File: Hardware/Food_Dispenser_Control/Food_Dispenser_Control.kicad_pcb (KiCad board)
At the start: 2 copper layers, 100 x 100 mm, 63 parts, among them J1 Motor Output, J10 Conn_01x03_Pin, J2 USB_C_Receptacle_USB2.0_16P, J3 Conn_01x02_Pin, J4 Conn_01x07_Pin, J5 Conn_01x01, J6 Conn_01x01, J7 Conn_01x04_Pin, J8 Motor Output, J9 Motor Output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

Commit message: Routing
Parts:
- moved SW6 26.6 mm to (128.0, 100.0)
- moved R30 26.5 mm to (123.0, 100.0), turned to 180 degrees
- moved C12 20.1 mm to (178.0, 130.5)
- moved C17 20.0 mm to (176.5, 111.0)
- moved C16 14.9 mm to (176.5, 113.2)
- moved C11 14.6 mm to (178.0, 133.0)
- moved R14 14.6 mm to (185.5, 133.0)
- moved C24 12.3 mm to (177.0, 97.0)
- moved C23 11.9 mm to (177.0, 94.5)
- moved C10 10.8 mm to (185.5, 135.5)
- moved C15 10.6 mm to (182.5, 114.0), turned to 90 degrees
- moved C3 10.3 mm to (155.0, 142.5), turned to 90 degrees
- moved C22 9.70 mm to (185.0, 93.5), turned to 90 degrees
- moved U8 9.69 mm to (179.5, 104.0)
- moved R21 9.67 mm to (185.0, 114.0), turned to 90 degrees
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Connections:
- J1 pad 1: Net-(J1-Pin_1) -> /AOUT1
- J1 pad 2: Net-(J1-Pin_2) -> /AOUT2
- J1 pad 3: Net-(J1-Pin_3) -> /BOUT2
- J1 pad 4: Net-(J1-Pin_4) -> /BOUT1
- J7 pad 2: /INA+ -> /INA-
- J7 pad 3: /INA- -> /INA+
- J8 pad 1: Net-(J8-Pin_1) -> /AOUT1_2
- J8 pad 2: Net-(J8-Pin_2) -> /AOUT2_2
- J8 pad 3: Net-(J8-Pin_3) -> /BOUT2_2
- J8 pad 4: Net-(J8-Pin_4) -> /BOUT1_2
- J9 pad 1: Net-(J9-Pin_1) -> /AOUT1_3
- J9 pad 2: Net-(J9-Pin_2) -> /AOUT2_3
- J9 pad 3: Net-(J9-Pin_3) -> /BOUT2_3
- J9 pad 4: Net-(J9-Pin_4) -> /BOUT1_3
- U5 pad 2: Net-(J1-Pin_4) -> /AOUT1
- U5 pad 4: Net-(J1-Pin_3) -> /AOUT2
- U5 pad 5: Net-(J1-Pin_1) -> /BOUT2
- U5 pad 7: Net-(J1-Pin_2) -> /BOUT1
- U6 pad 2: Net-(J8-Pin_4) -> /AOUT1_2
- U6 pad 4: Net-(J8-Pin_3) -> /AOUT2_2
- U6 pad 5: Net-(J8-Pin_1) -> /BOUT2_2
- U6 pad 7: Net-(J8-Pin_2) -> /BOUT1_2
- U8 pad 2: Net-(J9-Pin_4) -> /AOUT1_3
- U8 pad 4: Net-(J9-Pin_3) -> /AOUT2_3
- U8 pad 5: Net-(J9-Pin_1) -> /BOUT2_3
- U8 pad 7: Net-(J9-Pin_2) -> /BOUT1_3
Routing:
- net +3.3V: track 0.00 -> 218.5 mm, vias 0 -> 5
- net /VBAT_SYS: track 0.00 -> 132.0 mm, vias 0 -> 4
- net /DIRA: track 0.00 -> 58.7 mm, vias 0 -> 4
- net /PWMA: track 0.00 -> 57.6 mm, vias 0 -> 4
- net /DIRB: track 0.00 -> 56.8 mm, vias 0 -> 4
- net /PWMB: track 0.00 -> 56.6 mm, vias 0 -> 4
- net /Sleep: track 0.00 -> 56.1 mm
- net /VBAT: track 0.00 -> 52.9 mm, vias 0 -> 2
- net /GPIO1_3: track 0.00 -> 52.8 mm
- net /GPIO1_2: track 0.00 -> 51.3 mm
- net /EN1: track 0.00 -> 50.1 mm
- net /GPIO1_1: track 0.00 -> 49.7 mm
- net /XSHUT3: track 0.00 -> 44.4 mm
- net /XSHUT2: track 0.00 -> 42.8 mm
- net /SDA: track 0.00 -> 41.5 mm
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
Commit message: Ground Plane
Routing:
- added copper zone on B.Cu, net GND
- added copper zone on F.Cu, net GND
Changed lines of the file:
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@@
 			(at -2.4 23.090001 0)
 			(layer "F.SilkS")
+			(hide yes)
 			(effects
 				(font
@@
 			(at 4.5 -8.439999 0)
 			(layer "F.SilkS")
+			(hide yes)
 			(effects
 				(font
@@
 			(at 0 -3.449999 0)
 			(layer "F.SilkS")
+			(hide yes)
 			(effects
 				(font
@@
 			(at 0 3.449999 0)
 			(layer "F.Fab")
+			(hide yes)
 			(effects
 				(font
@@
 		(net 86)
 	)
+	(zone
+		(net 1)
+		(net_name "GND")
+		(layer "F.Cu")
+		(hatch edge 0.5)
+		(connect_pads
+			(clearance 0.5)
+		)
+		(min_thickness 0.25)
+		(filled_areas_thickness no)
+		(fill yes
+			(thermal_gap 0.5)
+			(thermal_bridge_width 0.5)
+		)
+		(polygon
+			(pts
+				(xy 101 158) (xy 101 58) (xy 201 58) (xy 201 158)
+			)
+		)
+	)
+	(zone
+		(net 1)
+		(net_name "GND")
+		(layer "B.Cu")
+		(hatch edge 0.5)
+		(priority 1)
+		(connect_pads
+			(clearance 0.5)
+		)
+		(min_thickness 0.25)
+		(filled_areas_thickness no)
+		(fill yes
+			(thermal_gap 0.5)
+			(thermal_bridge_width 0.5)
+		)
+		(polygon
+			(pts
+				(xy 101 158) (xy 101 58) (xy 201 58) (xy 201 158)
+			)
+		)
+	)
 	(embedded_fonts no)

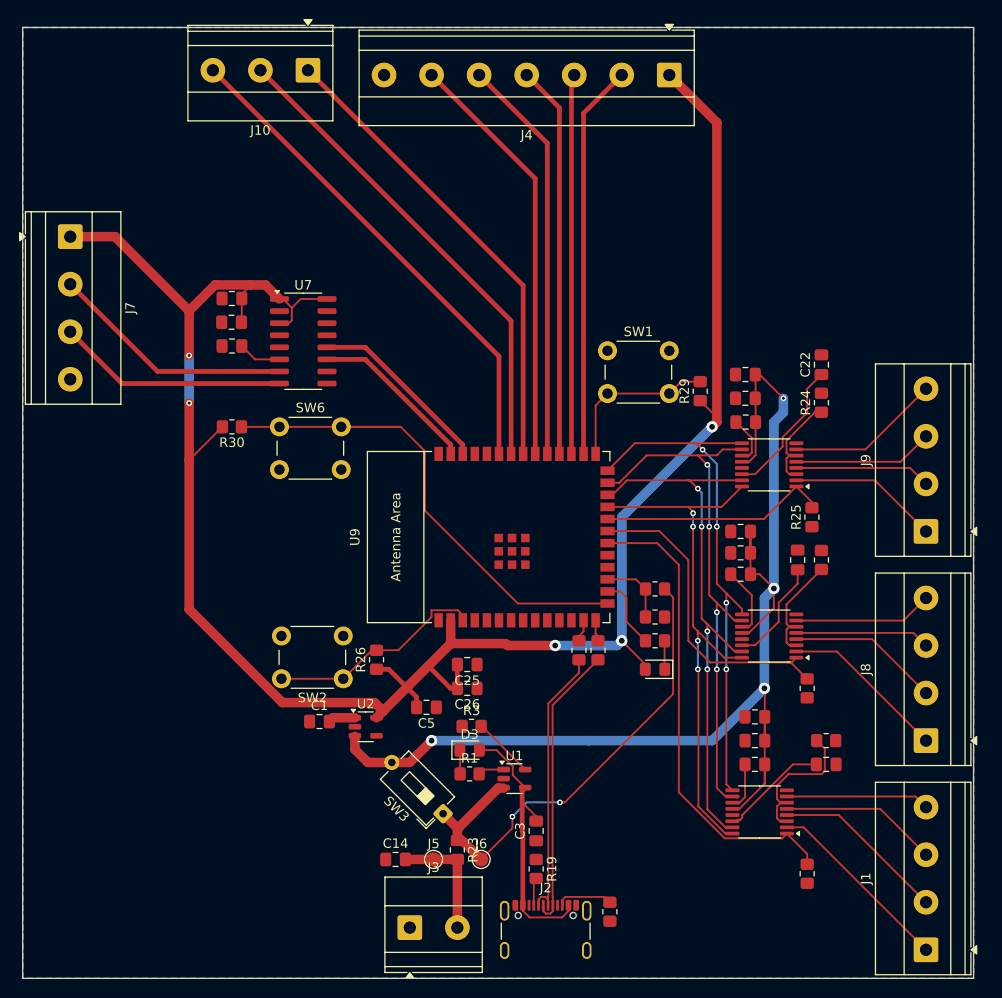
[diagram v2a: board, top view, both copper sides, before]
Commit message: Ground routing
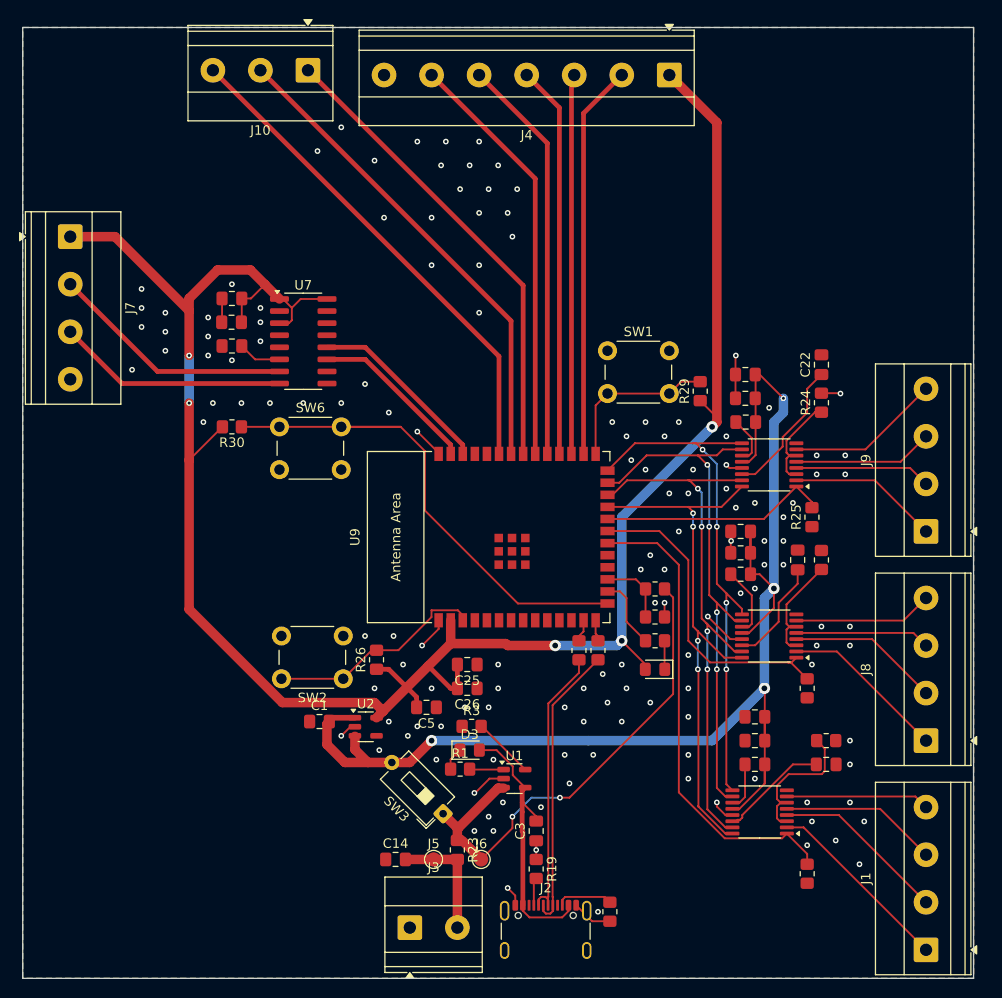
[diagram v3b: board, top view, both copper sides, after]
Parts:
- moved R1 1.12 mm to (147.0, 136.0)
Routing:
- net GND: track 0.00 -> 42.1 mm, vias 0 -> 142
- net /VBAT_SYS: track 132.0 -> 139.6 mm
- net +3.3V: track 218.5 -> 222.3 mm
- net Net-(U1-STAT): track 2.76 -> 3.59 mm

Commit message: updated hardware
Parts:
- added H1: MountingHole, MountingHole:MountingHole_3.2mm_M3, F.Cu at (196.0, 63.0)
- added H2: MountingHole, MountingHole:MountingHole_3.2mm_M3, F.Cu at (106.0, 63.0)
- added H3: MountingHole, MountingHole:MountingHole_3.2mm_M3, F.Cu at (106.0, 153.0)
- added H4: MountingHole, MountingHole:MountingHole_3.2mm_M3, F.Cu at (175.0, 153.5)
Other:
- board text added: "Team 62 NuChef"
